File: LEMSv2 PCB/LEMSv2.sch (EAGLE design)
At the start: 22 parts, among them U1 ADS1015

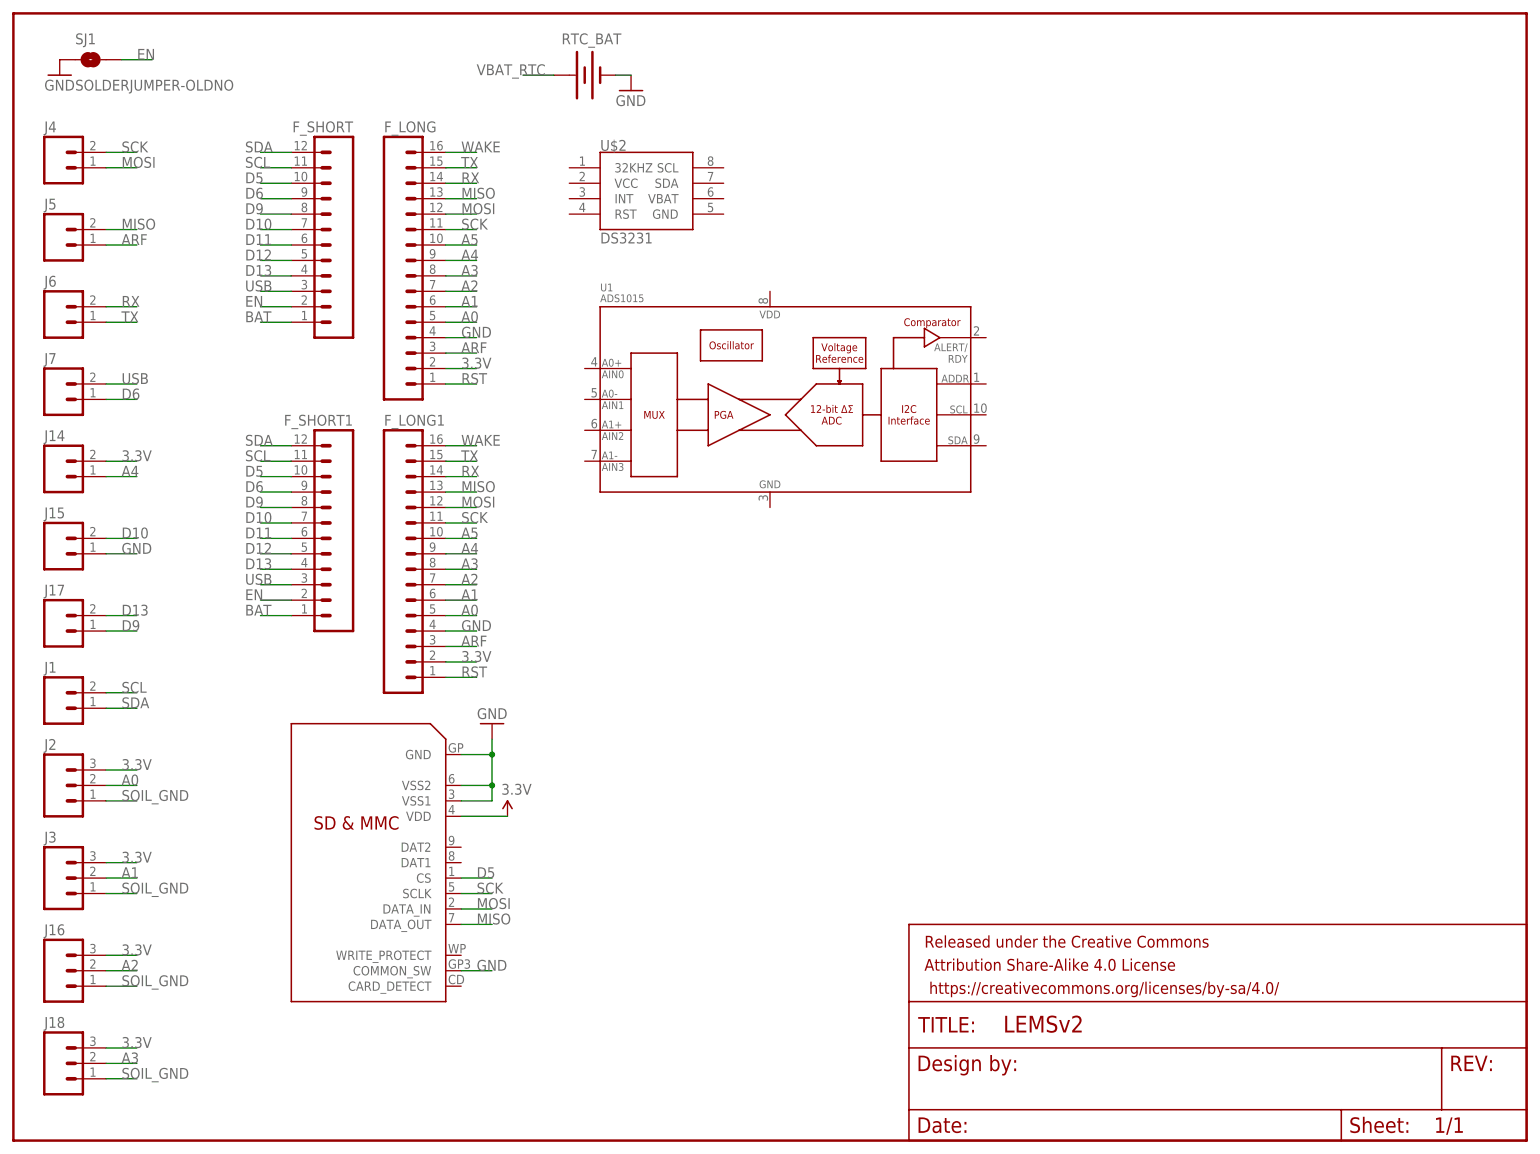
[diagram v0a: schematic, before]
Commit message: Changed how parts were added to BOM
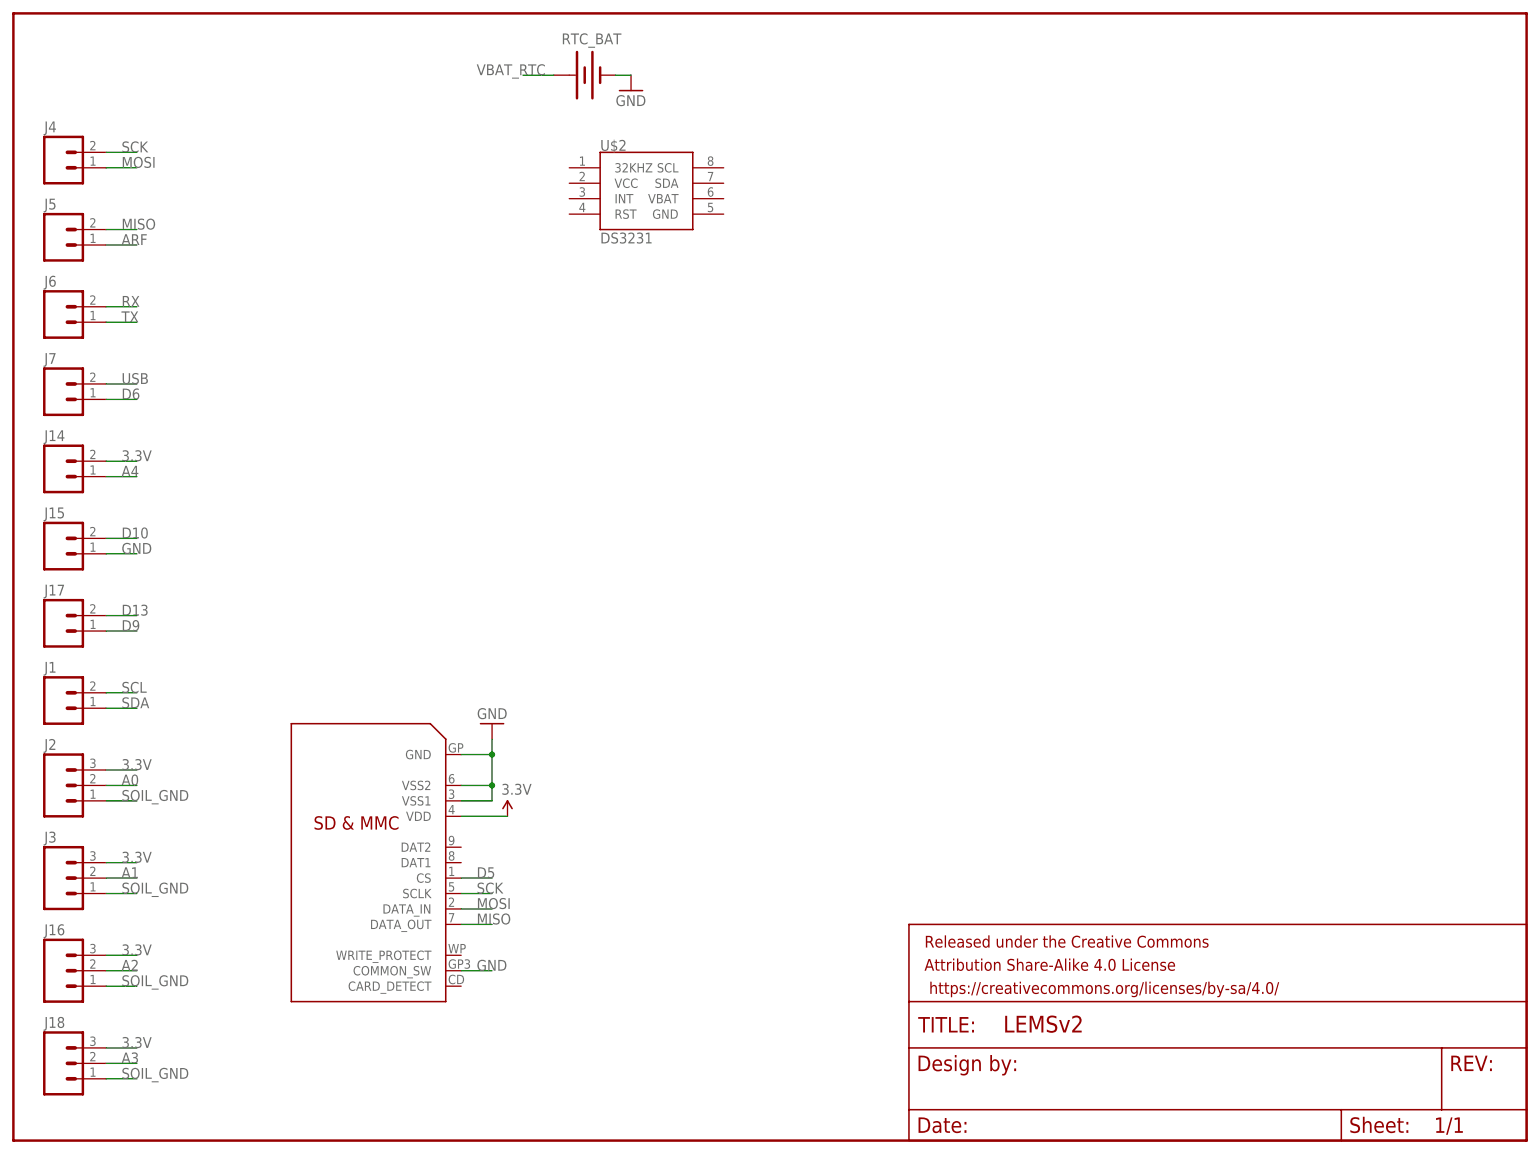
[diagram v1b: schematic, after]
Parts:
- removed F_LONG, F_LONG1: (no value), LEMSv2:M16PTH
- removed F_SHORT, F_SHORT1: (no value), LEMSv2:M12PTH
- removed SJ1: SOLDERJUMPER-OLDNO, LEMSv2:SOLDERJUMPER-OLDNO
- removed U1: ADS1015, SparkFun-AnalogIC:ADS1015
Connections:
- removed net A5: F_LONG.10, F_LONG1.10
- removed net BAT: F_SHORT.1, F_SHORT1.1
- removed net D11: F_SHORT.6, F_SHORT1.6
- removed net D12: F_SHORT.5, F_SHORT1.5
- removed net EN: F_SHORT.2, F_SHORT1.2, SJ1.2
- removed net RST: F_LONG.1, F_LONG1.1
- removed net WAKE: F_LONG.16, F_LONG1.16
- net 3.3V: no longer F_LONG.2, F_LONG1.2
- net A0: no longer F_LONG.5, F_LONG1.5
- net A1: no longer F_LONG.6, F_LONG1.6
- net A2: no longer F_LONG.7, F_LONG1.7
- net A3: no longer F_LONG.8, F_LONG1.8
- net A4: no longer F_LONG.9, F_LONG1.9
- net ARF: no longer F_LONG.3, F_LONG1.3
- net D10: no longer F_SHORT.7, F_SHORT1.7
- net D13: no longer F_SHORT.4, F_SHORT1.4
- net D5: no longer F_SHORT.10, F_SHORT1.10
- net D6: no longer F_SHORT.9, F_SHORT1.9
- net D9: no longer F_SHORT.8, F_SHORT1.8
- net GND: no longer F_LONG.4, F_LONG1.4, SJ1.1
- net MISO: no longer F_LONG.13, F_LONG1.13
- net MOSI: no longer F_LONG.12, F_LONG1.12
- net RX: no longer F_LONG.14, F_LONG1.14
- net SCK: no longer F_LONG.11, F_LONG1.11
- net SCL: no longer F_SHORT.11, F_SHORT1.11
- net SDA: no longer F_SHORT.12, F_SHORT1.12
- net TX: no longer F_LONG.15, F_LONG1.15
- net USB: no longer F_SHORT.3, F_SHORT1.3

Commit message: Determined more parts, added to lib/schematic
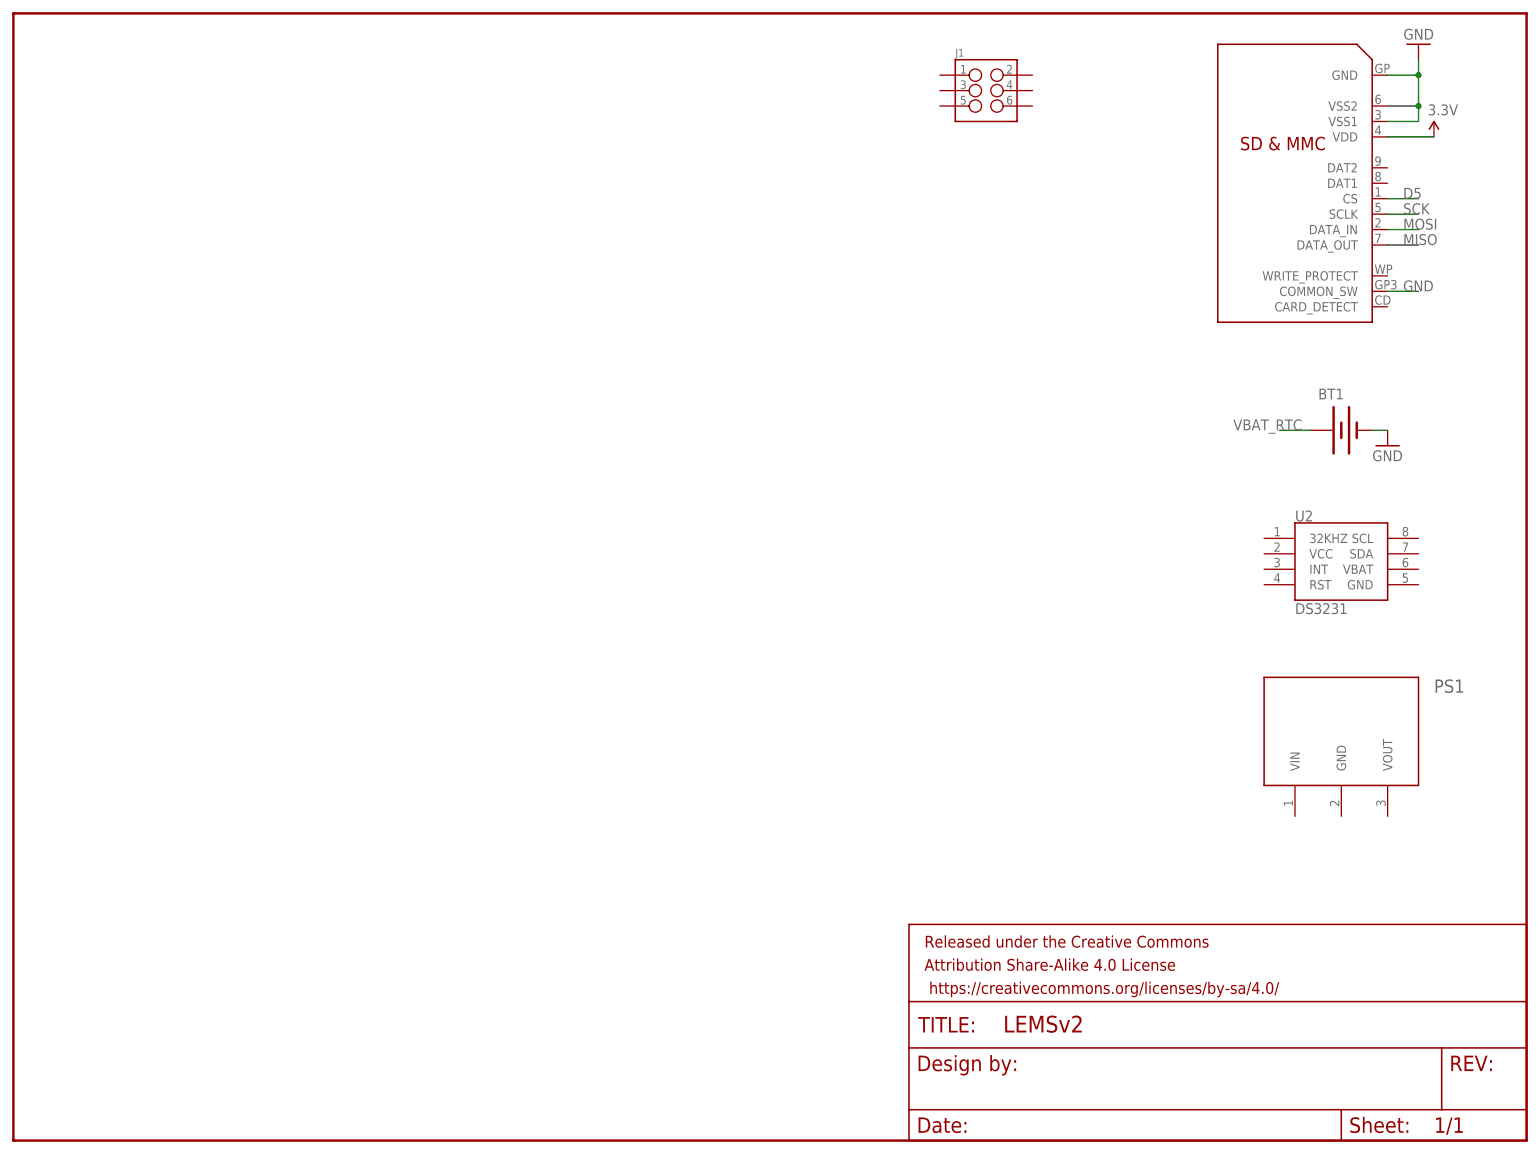
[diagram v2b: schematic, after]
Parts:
- removed J14, J15, J17, J4, J5, J6, J7: (no value), LEMSv2:M023.5MM
- removed J16, J18, J2, J3: (no value), LEMSv2:M03SCREW
- removed RTC_BAT: (no value), LEMSv2:BATTERY12MM
- removed U$1: SDMMC06132, LEMSv2:SDMMC06132
- removed U$2: DS3231, LEMSv2:DS3231
- added BT1: (no value), LEMSv2:BATTERY12MM
- added PS1: (no value), LEMSv2:TSR_1-2450
- added U1: SDMMC06132, LEMSv2:SDMMC06132
- added U2: DS3231, LEMSv2:DS3231
- J1: device LEMSv2:M023.5MM -> LEMSv2:M03X2FEMALE_SMD
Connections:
- removed net A0: J2.2
- removed net A1: J3.2
- removed net A2: J16.2
- removed net A3: J18.2
- removed net A4: J14.1
- removed net ARF: J5.1
- removed net D10: J15.2
- removed net D13: J17.2
- removed net D6: J7.1
- removed net D9: J17.1
- removed net RX: J6.2
- removed net SCL: J1.2
- removed net SDA: J1.1
- removed net SOIL_GND: J16.1, J18.1, J2.1, J3.1
- removed net TX: J6.1
- removed net USB: J7.2
- net 3.3V: now also U1.VDD; no longer J14.2, J16.3, J18.3, J2.3, J3.3, U$1.VDD
- net D5: now also U1.CS; no longer U$1.CS
- net GND: now also BT1.-, U1.COMMON_SW, U1.GND, U1.VSS1, U1.VSS2; no longer J15.1, RTC_BAT.-, U$1.COMMON_SW, U$1.GND, U$1.VSS1, U$1.VSS2
- net MISO: now also U1.DATA_OUT; no longer J5.2, U$1.DATA_OUT
- net MOSI: now also U1.DATA_IN; no longer J4.1, U$1.DATA_IN
- net SCK: now also U1.SCLK; no longer J4.2, U$1.SCLK
- net VBAT_RTC: now also BT1.+; no longer RTC_BAT.+

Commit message: Improved BOM and added parts
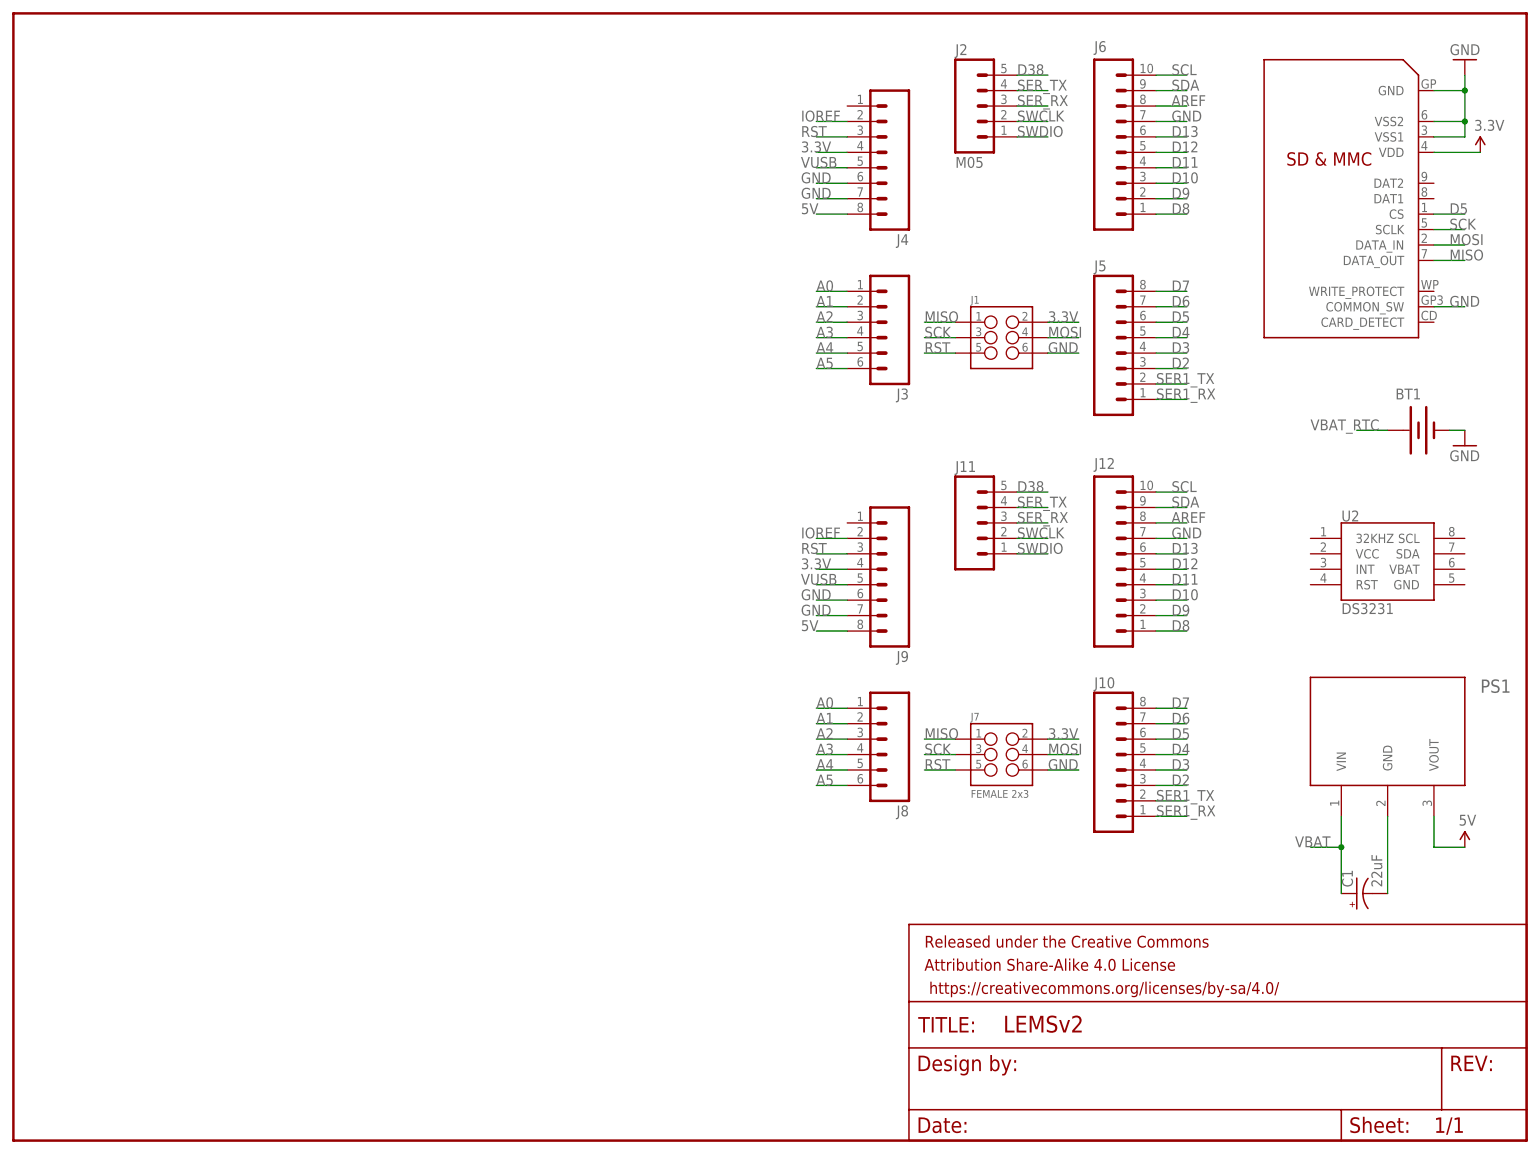
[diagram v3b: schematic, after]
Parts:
- added C1: 22uF, LEMSv2:CAP_POLPTH2
- added J10, J9: (no value), LEMSv2:M08LOCK
- added J11: (no value), LEMSv2:M05_SFLOCK
- added J12: (no value), LEMSv2:M10LOCK
- added J2: M05, LEMSv2:M05
- added J3: (no value), LEMSv2:M06SMD-STRAIGHT-COMBO-FEMALE
- added J4, J5: (no value), LEMSv2:M08SMD-COMBO-FEMALE
- added J6: (no value), LEMSv2:M10SMD_COMBO-FEMALE
- added J7: FEMALE 2x3, LEMSv2:M03X2FEMALE
- added J8: (no value), LEMSv2:M06LOCK
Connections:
- new net 5V: J4.8, J9.8, PS1.VOUT
- new net A0: J3.1, J8.1
- new net A1: J3.2, J8.2
- new net A2: J3.3, J8.3
- new net A3: J3.4, J8.4
- new net A4: J3.5, J8.5
- new net A5: J3.6, J8.6
- new net AREF: J12.8, J6.8
- new net D10: J12.3, J6.3
- new net D11: J12.4, J6.4
- new net D12: J12.5, J6.5
- new net D13: J12.6, J6.6
- new net D2: J10.3, J5.3
- new net D3: J10.4, J5.4
- new net D38: J11.5, J2.5
- new net D4: J10.5, J5.5
- new net D6: J10.7, J5.7
- new net D7: J10.8, J5.8
- new net D8: J12.1, J6.1
- new net D9: J12.2, J6.2
- new net IOREF: J4.2, J9.2
- new net RST: J1.5, J4.3, J7.5, J9.3
- new net SCL: J12.10, J6.10
- new net SDA: J12.9, J6.9
- new net SER1_RX: J10.1, J5.1
- new net SER1_TX: J10.2, J5.2
- new net SER_RX: J11.3, J2.3
- new net SER_TX: J11.4, J2.4
- new net SWCLK: J11.2, J2.2
- new net SWDIO: J11.1, J2.1
- new net VBAT: C1.+, PS1.VIN
- new net VUSB: J4.5, J9.5
- net 3.3V: now also J1.2, J4.4, J7.2, J9.4
- net D5: now also J10.6, J5.6
- net GND: now also C1.-, J1.6, J12.7, J4.6, J4.7, J6.7, J7.6, J9.6, J9.7, PS1.GND
- net MISO: now also J1.1, J7.1
- net MOSI: now also J1.4, J7.4
- net SCK: now also J1.3, J7.3
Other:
- moved on the sheet: BT1, J1, PS1, U2
